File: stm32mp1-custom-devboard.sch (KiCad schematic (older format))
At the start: 0 parts

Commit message: Finished work at st-link, figurated elements on pcb
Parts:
- added P1: Main Power Supply, Smd_Connectors:2060-452_998-404, symbol Smd_Connectors:2060-452_998-404
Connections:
- net Power Supply Module/POWER_IN_7_TO_18V: now also P1.2
- net Power Supply Module/POWER_IN_GND: now also P1.1
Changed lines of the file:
@@
 	7450 1700 7350 1700
 $Sheet
-S 10600 3900 1850 1500
+S 4400 4400 1850 1500
 U 60087A46
 F0 "Arduino Shield Module" 50
@@
 $EndSheet
 $Sheet
-S 10600 5600 1850 1550
-U 5FDFB166
-F0 "STLink Module" 50
-F1 "stlink.sch" 50
-$EndSheet
-$Sheet
-S 12750 3900 1850 1500
+S 4400 2600 1850 1500
 U 5FFEC95A
 F0 "MiniPci Module" 50
 F1 "minipci_module.sch" 50
 $EndSheet
+$Sheet
+S 10600 4050 1850 1550
+U 5FDFB166
+F0 "STLink Module" 50
+F1 "stlink.sch" 50
+F2 "POWER_IN_5V" I R 12450 4150 50
+F3 "POWER_IN_GND" I R 12450 4250 50
+F4 "STLINK_TX" O L 10600 4150 50
+F5 "STLINK_RX" O L 10600 4250 50
+F6 "JTCK" O L 10600 4850 50
+F7 "JTDO" O L 10600 4950 50
+F8 "JTDI" I L 10600 5050 50
+F9 "STLINK-SWO" I L 10600 4450 50
+F10 "STLINK-SWCLK" I L 10600 4550 50
+F11 "STLINK-SWDIO" I L 10600 4650 50
+F12 "JTRST" I L 10600 5150 50
+F13 "STM-JTMS-SWDIO" I R 12450 5150 50
+F14 "STM-JTCK-SWCLK" I R 12450 5250 50
+F15 "J_TMS" I L 10600 5250 50
+$EndSheet
+$Comp
+L Smd_Connectors:2060-452_998-404 P1
+U 1 1 600C8833
+P 3850 1750
+F 0 "P1" H 3850 1600 50  0000 C CNN
+F 1 "Main Power Supply" V 4050 1700 50  0000 C CNN
+F 2 "Smd_Connectors:2060-452_998-404" H 3850 1550 60  0001 C CNN
+F 3 "Connectors/Smd_Connectors/Components_Documentation/WAGO_2060_51300133.pdf" H 3850 1550 60  0001 C CNN
+F 4 "WAGO" H 3850 1750 50  0001 C CNN "Manufacturer"
+F 5 "2060-452/998-404" H 3850 1750 50  0001 C CNN "Manufacturer Part Number"
+F 6 "TME" H 3850 1750 50  0001 C CNN "Supplier"
+F 7 "2060-452/998-404" H 3850 1750 50  0001 C CNN "Supplier Part Number"
+F 8 "https://www.tme.eu/pl/details/2060-452_998-404/zlacza-do-led/wago/2060-452-998-404/" H 3850 1750 50  0001 C CNN "URL"
+F 9 "4,5708" H 3850 1750 50  0001 C CNN "Price@1pc"
+F 10 "2,9563" H 3850 1750 50  0001 C CNN "Price@1000pcs"
+F 11 "WP" H 3850 1750 50  0001 C CNN "Developer"
+	1    3850 1750
+	-1   0    0    1
+$EndComp
+Wire Wire Line
+	4200 1700 4400 1700
+Wire Wire Line
+	4200 1800 4400 1800
 $EndSCHEMATC

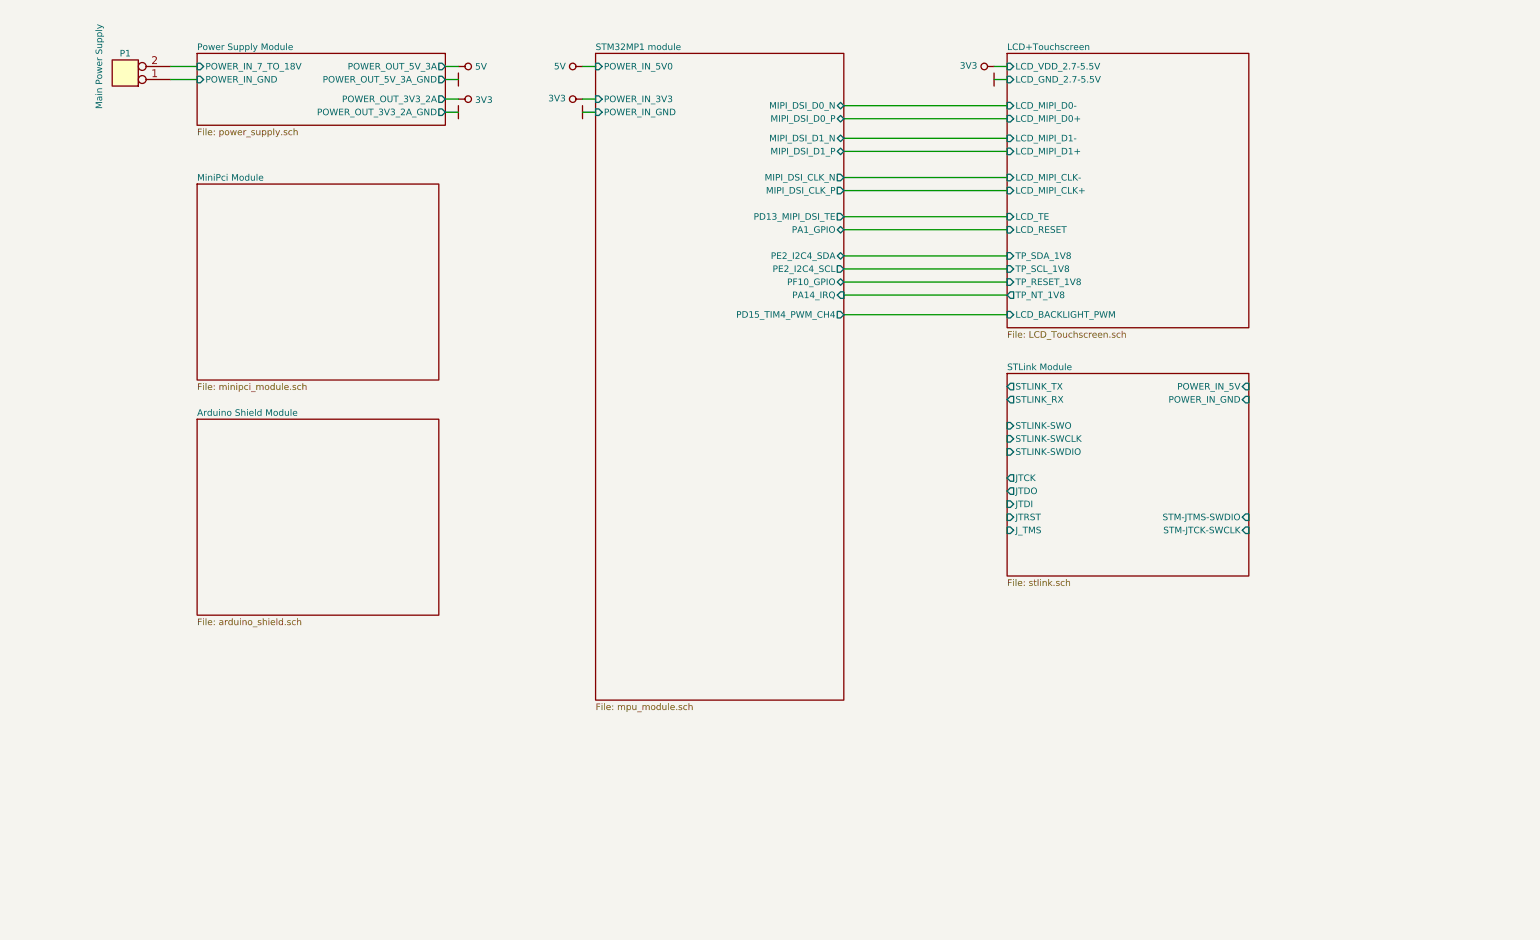
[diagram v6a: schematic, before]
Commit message: Added ethernet and usb module
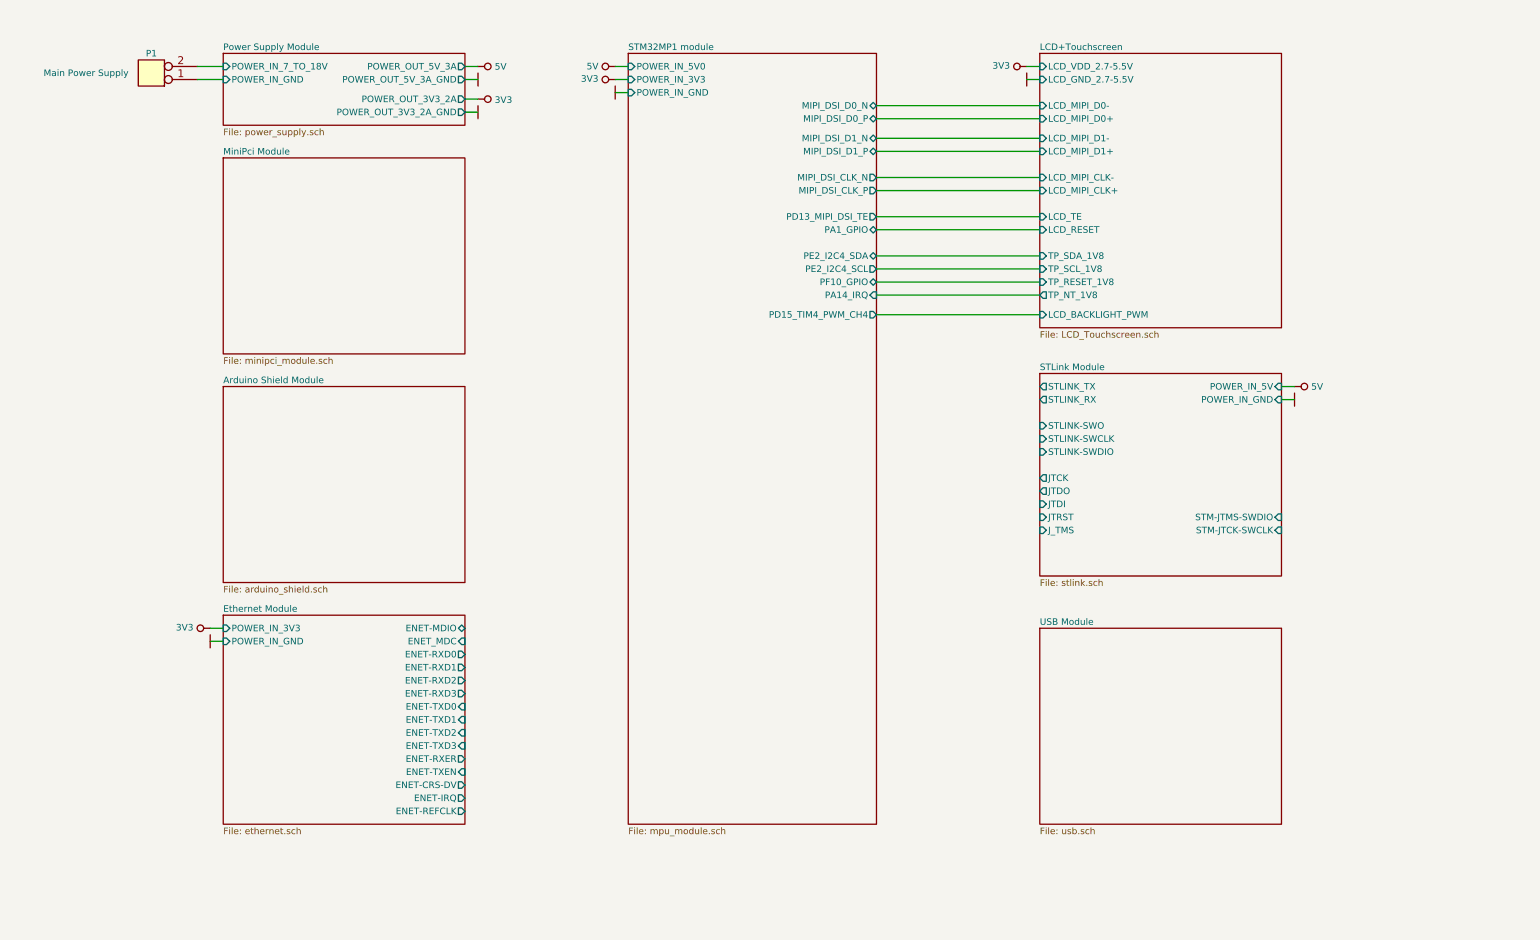
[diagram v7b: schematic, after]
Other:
- moved on the sheet: P1

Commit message: Added new USB connectors on schematic, figurated elements on pcb
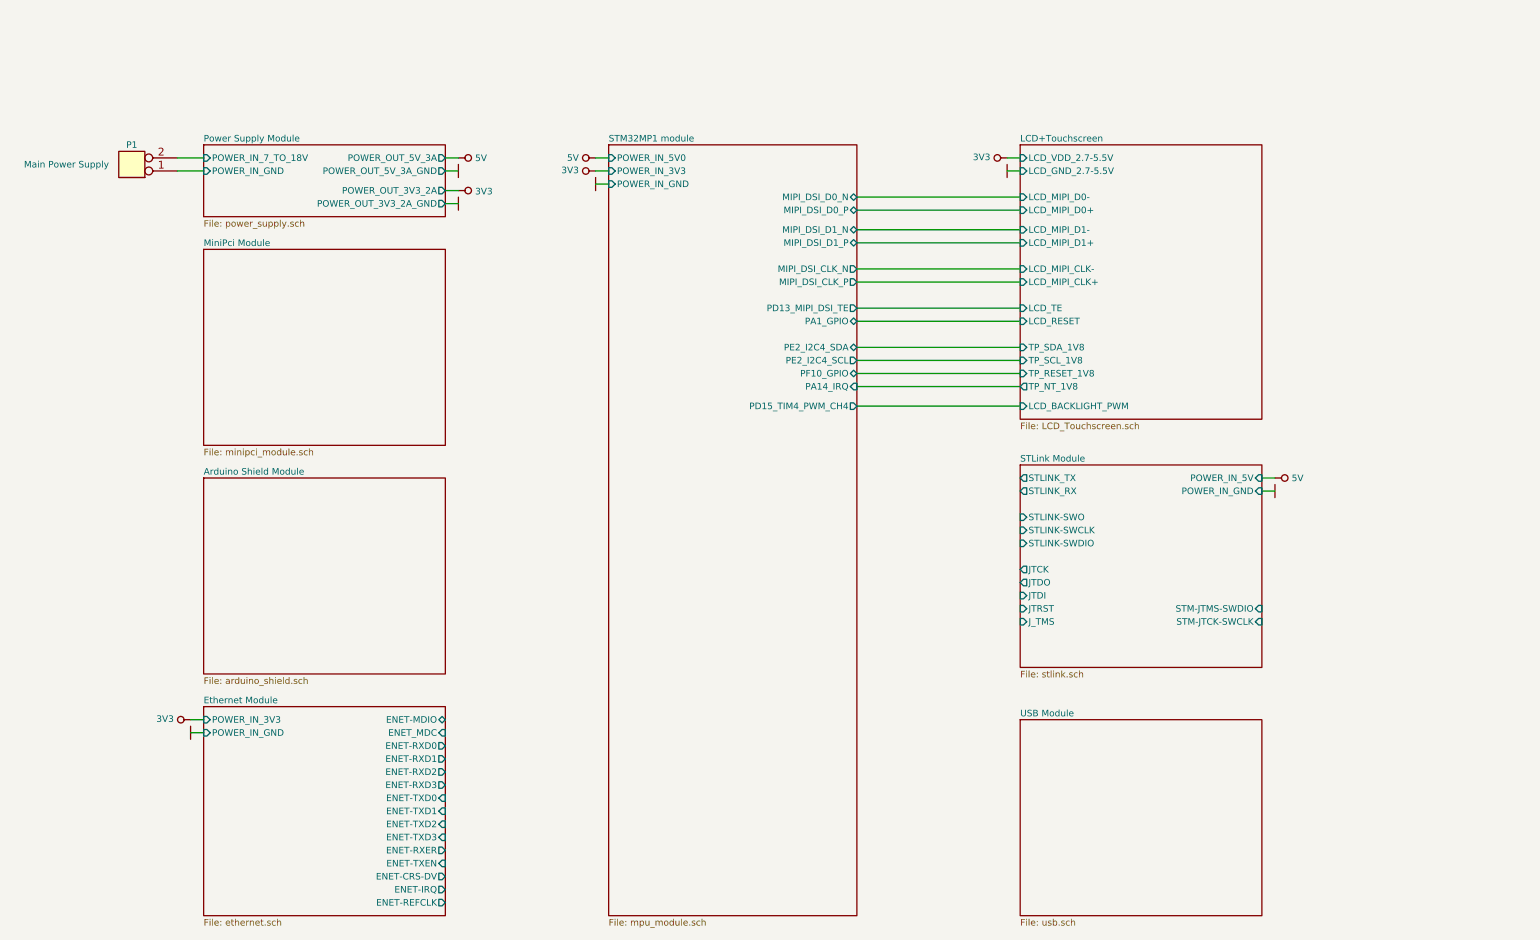
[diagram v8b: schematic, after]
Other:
- moved on the sheet: P1
